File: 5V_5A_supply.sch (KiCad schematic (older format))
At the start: 14 parts, among them U2 TPS54561

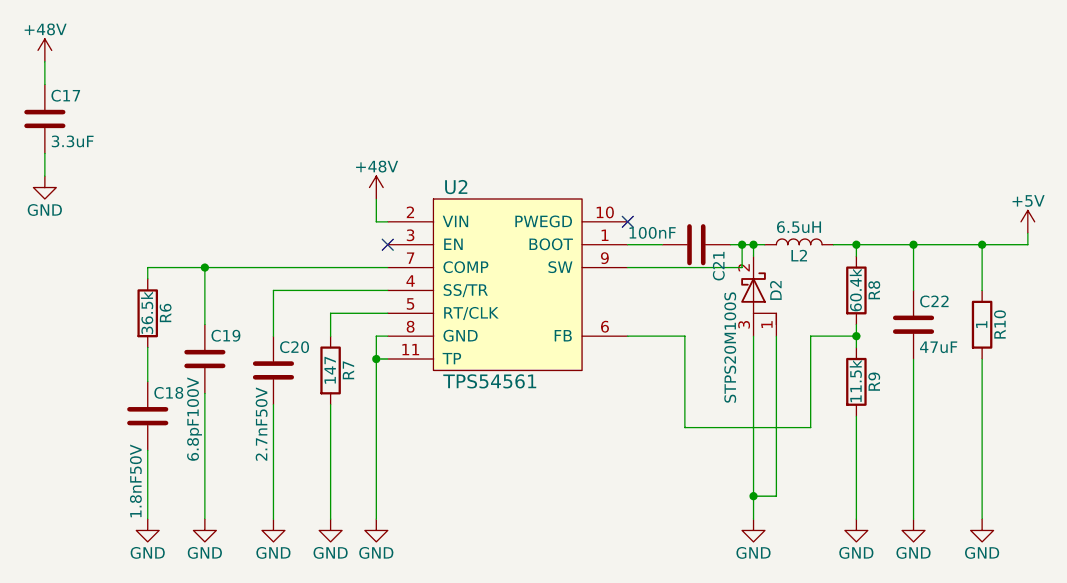
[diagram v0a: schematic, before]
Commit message: add MPN and change footprints
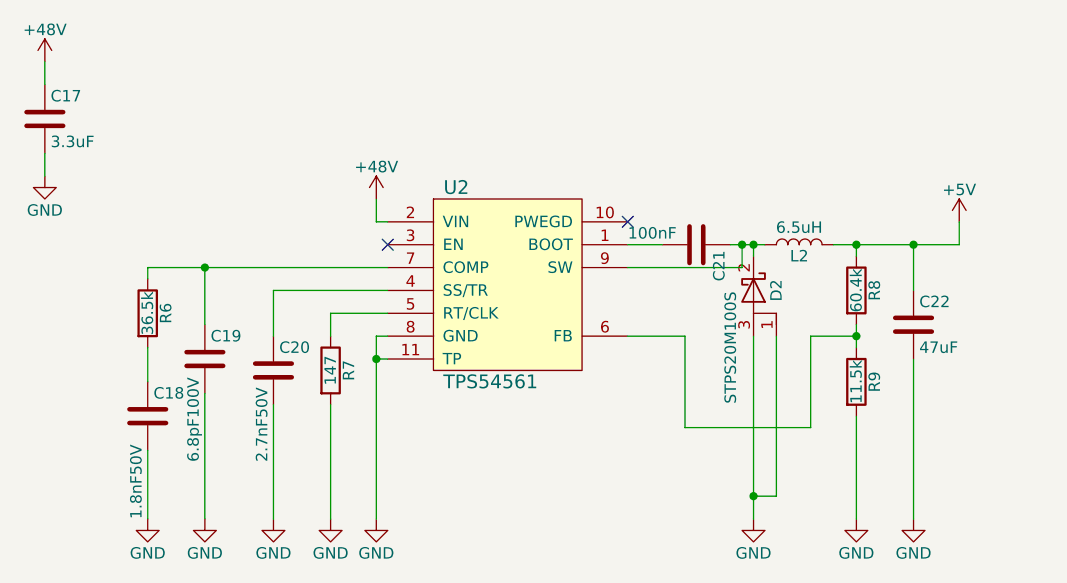
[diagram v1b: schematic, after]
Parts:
- removed R10: 1, Resistors_SMD:R_0402, symbol R
- C17: footprint Capacitors_SMD:C_1206 -> Capacitors_SMD:C_1210; MPN (none) -> 2211157
- C18: MPN (none) -> 2678141
- C19: footprint Capacitors_SMD:C_0402 -> Capacitors_SMD:C_0603; MPN (none) -> 1865503
- C20: footprint Capacitors_SMD:C_0805 -> Capacitors_SMD:C_0603; MPN (none) -> 2680086
- C21: MPN (none) -> 2690952
- C22: footprint Capacitors_SMD:C_1210 -> Capacitors_SMD:C_0603; MPN (none) -> 2346908
- D2: MPN (none) -> 2325907
- L2: MPN (none) -> 2211621
- R6: MPN (none) -> 2072974
- R7: MPN (none) -> 1802949
- R8: MPN (none) -> 1652810
- R9: MPN (none) -> 1803142
- U2: MPN (none) -> TPS54561DPRT
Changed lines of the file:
@@
 LIBS:contrib
 LIBS:valves
+LIBS:MB_DEVICE
 LIBS:power_board-cache
 EELAYER 25 0
@@
 F 2 "MB_LIB:TPS54561" H 5450 3400 60  0001 C CNN
 F 3 "" H 5450 3400 60  0001 C CNN
+F 4 "TPS54561DPRT" H 5450 3400 60  0001 C CNN "MPN"
 	1    5450 3400
 	1    0    0    -1
@@
 Connection ~ 4900 3650
 $Comp
-L GND #PWR036
+L GND #PWR045
 U 1 1 5AA70352
 P 4900 4350
-F 0 "#PWR036" H 4900 4100 50  0001 C CNN
+F 0 "#PWR045" H 4900 4100 50  0001 C CNN
 F 1 "GND" H 4900 4200 50  0000 C CNN
 F 2 "" H 4900 4350 50  0001 C CNN
@@
 F 0 "C17" H 3475 2700 50  0000 L CNN
 F 1 "3.3uF" H 3475 2500 50  0000 L CNN
-F 2 "Capacitors_SMD:C_1206" H 3488 2450 50  0001 C CNN
+F 2 "Capacitors_SMD:C_1210" H 3488 2450 50  0001 C CNN
 F 3 "" H 3450 2600 50  0001 C CNN
+F 4 "2211157" H 3450 2600 60  0001 C CNN "MPN"
 	1    3450 2600
 	1    0    0    -1
@@
 F 2 "Capacitors_SMD:C_0402" H 3938 3750 50  0001 C CNN
 F 3 "" H 3900 3900 50  0001 C CNN
+F 4 "2678141" H 3900 3900 60  0001 C CNN "MPN"
 	1    3900 3900
 	1    0    0    -1
@@
 F 0 "C19" H 4175 3750 50  0000 L CNN
 F 1 "6.8pF100V" V 4100 3200 50  0000 L CNN
-F 2 "Capacitors_SMD:C_0402" H 4188 3500 50  0001 C CNN
+F 2 "Capacitors_SMD:C_0603" H 4188 3500 50  0001 C CNN
 F 3 "" H 4150 3650 50  0001 C CNN
+F 4 "1865503" H 4150 3650 60  0001 C CNN "MPN"
 	1    4150 3650
 	1    0    0    -1
@@
 F 0 "C20" H 4475 3800 50  0000 L CNN
 F 1 "2.7nF50V" V 4400 3300 50  0000 L CNN
-F 2 "Capacitors_SMD:C_0805" H 4488 3550 50  0001 C CNN
+F 2 "Capacitors_SMD:C_0603" H 4488 3550 50  0001 C CNN
 F 3 "" H 4450 3700 50  0001 C CNN
+F 4 "2680086" H 4450 3700 60  0001 C CNN "MPN"
 	1    4450 3700
 	1    0    0    -1
@@
 F 2 "Resistors_SMD:R_0402" V 3830 3450 50  0001 C CNN
 F 3 "" H 3900 3450 50  0001 C CNN
+F 4 "2072974" V 3900 3450 60  0001 C CNN "MPN"
 	1    3900 3450
 	1    0    0    -1
@@
 F 2 "Resistors_SMD:R_0402" V 4630 3700 50  0001 C CNN
 F 3 "" H 4700 3700 50  0001 C CNN
+F 4 "1802949" V 4700 3700 60  0001 C CNN "MPN"
 	1    4700 3700
 	1    0    0    -1
@@
 F 2 "Capacitors_SMD:C_0402" H 6338 3000 50  0001 C CNN
 F 3 "" H 6300 3150 50  0001 C CNN
+F 4 "2690952" H 6300 3150 60  0001 C CNN "MPN"
 	1    6300 3150
 	0    1    1    0
@@
 F 2 "Resistors_SMD:R_0402" V 6930 3350 50  0001 C CNN
 F 3 "" H 7000 3350 50  0001 C CNN
+F 4 "1652810" V 7000 3350 60  0001 C CNN "MPN"
 	1    7000 3350
 	1    0    0    -1
@@
 F 2 "Resistors_SMD:R_0402" V 6930 3750 50  0001 C CNN
 F 3 "" H 7000 3750 50  0001 C CNN
+F 4 "1803142" V 7000 3750 60  0001 C CNN "MPN"
 	1    7000 3750
 	1    0    0    -1
 $EndComp
 $Comp
-L +48V #PWR037
+L +48V #PWR046
 U 1 1 5AA7035C
 P 3450 2350
-F 0 "#PWR037" H 3450 2200 50  0001 C CNN
+F 0 "#PWR046" H 3450 2200 50  0001 C CNN
 F 1 "+48V" H 3450 2490 50  0000 C CNN
 F 2 "" H 3450 2350 50  0001 C CNN
@@
 $EndComp
 $Comp
-L +48V #PWR038
+L +48V #PWR047
 U 1 1 5AA7035D
 P 4900 2950
-F 0 "#PWR038" H 4900 2800 50  0001 C CNN
+F 0 "#PWR047" H 4900 2800 50  0001 C CNN
 F 1 "+48V" H 4900 3090 50  0000 C CNN
 F 2 "" H 4900 2950 50  0001 C CNN
@@
 $EndComp
 $Comp
-L GND #PWR039
+L GND #PWR048
 U 1 1 5AA7035E
 P 3450 2850
-F 0 "#PWR039" H 3450 2600 50  0001 C CNN
+F 0 "#PWR048" H 3450 2600 50  0001 C CNN
 F 1 "GND" H 3450 2700 50  0000 C CNN
 F 2 "" H 3450 2850 50  0001 C CNN
@@
 	4700 3850 4700 4350
 $Comp
-L GND #PWR040
+L GND #PWR049
 U 1 1 5AA7035F
 P 4700 4350
-F 0 "#PWR040" H 4700 4100 50  0001 C CNN
+F 0 "#PWR049" H 4700 4100 50  0001 C CNN
 F 1 "GND" H 4700 4200 50  0000 C CNN
 F 2 "" H 4700 4350 50  0001 C CNN
@@
 $EndComp
 $Comp
-L GND #PWR041
+L GND #PWR050
 U 1 1 5AA70360
 P 4450 4350
-F 0 "#PWR041" H 4450 4100 50  0001 C CNN
+F 0 "#PWR050" H 4450 4100 50  0001 C CNN
 F 1 "GND" H 4450 4200 50  0000 C CNN
 F 2 "" H 4450 4350 50  0001 C CNN
@@
 $EndComp
 $Comp
-L GND #PWR042
+L GND #PWR051
 U 1 1 5AA70361
 P 4150 4350
-F 0 "#PWR042" H 4150 4100 50  0001 C CNN
+F 0 "#PWR051" H 4150 4100 50  0001 C CNN
 F 1 "GND" H 4150 4200 50  0000 C CNN
 F 2 "" H 4150 4350 50  0001 C CNN
@@
 $EndComp
 $Comp
-L GND #PWR043
+L GND #PWR052
 U 1 1 5AA70362
 P 3900 4350
-F 0 "#PWR043" H 3900 4100 50  0001 C CNN
+F 0 "#PWR052" H 3900 4100 50  0001 C CNN
 F 1 "GND" H 3900 4200 50  0000 C CNN
 F 2 "" H 3900 4350 50  0001 C CNN
@@
 F 2 "Inductors_SMD:L_Wuerth_HCI-1050" H 6750 3150 50  0001 C CNN
 F 3 "http://katalog.we-online.de/pbs/datasheet/744325650.pdf" H 6750 3150 50  0001 C CNN
+F 4 "2211621" V 6750 3150 60  0001 C CNN "MPN"
 	1    6750 3150
 	0    -1   -1   0
@@
 Connection ~ 7000 3150
 Wire Wire Line
-	6900 3150 7750 3150
+	6900 3150 7450 3150
 Wire Wire Line
 	7250 3150 7250 3350
 Wire Wire Line
 	7250 3650 7250 4350
-$Comp
-L R R10
-U 1 1 5AA70366
-P 7550 3500
-F 0 "R10" V 7630 3500 50  0000 C CNN
-F 1 "1" V 7550 3500 50  0000 C CNN
-F 2 "Resistors_SMD:R_0402" V 7480 3500 50  0001 C CNN
-F 3 "" H 7550 3500 50  0001 C CNN
-	1    7550 3500
-	1    0    0    -1
-$EndComp
-Wire Wire Line
-	7550 3150 7550 3350
 Connection ~ 7250 3150
-Wire Wire Line
-	7550 3650 7550 4350
 Wire Wire Line
 	6000 3250 6500 3250
@@
 Connection ~ 6550 3150
 $Comp
-L GND #PWR044
+L GND #PWR053
 U 1 1 5AA70368
 P 6550 4350
-F 0 "#PWR044" H 6550 4100 50  0001 C CNN
+F 0 "#PWR053" H 6550 4100 50  0001 C CNN
 F 1 "GND" H 6550 4200 50  0000 C CNN
 F 2 "" H 6550 4350 50  0001 C CNN
@@
 	7000 3900 7000 4350
 $Comp
-L GND #PWR045
+L GND #PWR054
 U 1 1 5AA70369
 P 7000 4350
-F 0 "#PWR045" H 7000 4100 50  0001 C CNN
+F 0 "#PWR054" H 7000 4100 50  0001 C CNN
 F 1 "GND" H 7000 4200 50  0000 C CNN
 F 2 "" H 7000 4350 50  0001 C CNN
@@
 $EndComp
 $Comp
-L GND #PWR046
+L GND #PWR055
 U 1 1 5AA7036A
 P 7250 4350
-F 0 "#PWR046" H 7250 4100 50  0001 C CNN
+F 0 "#PWR055" H 7250 4100 50  0001 C CNN
 F 1 "GND" H 7250 4200 50  0000 C CNN
 F 2 "" H 7250 4350 50  0001 C CNN
@@
 	1    0    0    -1
 $EndComp
-$Comp
-L GND #PWR047
-U 1 1 5AA7036B
-P 7550 4350
-F 0 "#PWR047" H 7550 4100 50  0001 C CNN
-F 1 "GND" H 7550 4200 50  0000 C CNN
-F 2 "" H 7550 4350 50  0001 C CNN
-F 3 "" H 7550 4350 50  0001 C CNN
-	1    7550 4350
-	1    0    0    -1
-$EndComp
-Wire Wire Line
-	7750 3150 7750 3100
-Connection ~ 7550 3150
+Wire Wire Line
+	7450 3150 7450 3050
 $Comp
 L C C22
@@
 F 0 "C22" H 7275 3600 50  0000 L CNN
 F 1 "47uF" H 7275 3400 50  0000 L CNN
-F 2 "Capacitors_SMD:C_1210" H 7288 3350 50  0001 C CNN
+F 2 "Capacitors_SMD:C_0603" H 7288 3350 50  0001 C CNN
 F 3 "" H 7250 3500 50  0001 C CNN
+F 4 "2346908" H 7250 3500 60  0001 C CNN "MPN"
 	1    7250 3500
 	1    0    0    -1
 $EndComp
 $Comp
-L +5V #PWR048
+L +5V #PWR056
 U 1 1 5AA707C6
-P 7750 3100
-F 0 "#PWR048" H 7750 2950 50  0001 C CNN
-F 1 "+5V" H 7750 3240 50  0000 C CNN
-F 2 "" H 7750 3100 50  0001 C CNN
-F 3 "" H 7750 3100 50  0001 C CNN
-	1    7750 3100
+P 7450 3050
+F 0 "#PWR056" H 7450 2900 50  0001 C CNN
+F 1 "+5V" H 7450 3190 50  0000 C CNN
+F 2 "" H 7450 3050 50  0001 C CNN
+F 3 "" H 7450 3050 50  0001 C CNN
+	1    7450 3050
 	1    0    0    -1
 $EndComp
@@
 F 2 "TO_SOT_Packages_SMD:TO-263-2" H 6550 3350 50  0001 C CNN
 F 3 "http://www.st.com/content/ccc/resource/technical/document/datasheet/group2/8f/d3/41/ea/82/b2/4b/5a/CD00228904/files/CD00228904.pdf/jcr:content/translations/en.CD00228904.pdf" H 6550 3350 50  0001 C CNN
+F 4 "2325907" H 6550 3350 60  0001 C CNN "MPN"
 	1    6550 3350
 	0    1    1    0

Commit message: mpn was changed
added needed conectors
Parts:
- C17: MPN 2211157 -> CGA6P3X7R1H335K250AB
- C18: MPN 2678141 -> C0402C182J5RACTU
- C19: MPN 1865503 -> C0603C689C1GACTU
- C20: MPN 2680086 -> C0603C272J5RACTU
- C21: MPN 2690952 -> 04025C104KAT2A
- C22: MPN 2346908 -> C1608X7R1H474K080AC
- D2: MPN 2325907 -> STPS20M100SG-TR
- L2: MPN 2211621 -> 744325650
- R6: MPN 2072974 -> MCMR04X3652FTL
- R7: MPN 1802949 -> MC00625W04021147R
- R8: MPN 1652810 -> CRCW040260K4FKED
- R9: MPN 1803142 -> MC00625W0402111K5
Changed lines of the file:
@@
 F 2 "Capacitors_SMD:C_1210" H 3488 2450 50  0001 C CNN
 F 3 "" H 3450 2600 50  0001 C CNN
-F 4 "2211157" H 3450 2600 60  0001 C CNN "MPN"
+F 4 "CGA6P3X7R1H335K250AB" H 3450 2600 60  0001 C CNN "MPN"
 	1    3450 2600
 	1    0    0    -1
@@
 F 2 "Capacitors_SMD:C_0402" H 3938 3750 50  0001 C CNN
 F 3 "" H 3900 3900 50  0001 C CNN
-F 4 "2678141" H 3900 3900 60  0001 C CNN "MPN"
+F 4 "C0402C182J5RACTU" H 3900 3900 60  0001 C CNN "MPN"
 	1    3900 3900
 	1    0    0    -1
@@
 F 2 "Capacitors_SMD:C_0603" H 4188 3500 50  0001 C CNN
 F 3 "" H 4150 3650 50  0001 C CNN
-F 4 "1865503" H 4150 3650 60  0001 C CNN "MPN"
+F 4 "C0603C689C1GACTU" H 4150 3650 60  0001 C CNN "MPN"
 	1    4150 3650
 	1    0    0    -1
@@
 F 2 "Capacitors_SMD:C_0603" H 4488 3550 50  0001 C CNN
 F 3 "" H 4450 3700 50  0001 C CNN
-F 4 "2680086" H 4450 3700 60  0001 C CNN "MPN"
+F 4 "C0603C272J5RACTU" H 4450 3700 60  0001 C CNN "MPN"
 	1    4450 3700
 	1    0    0    -1
@@
 F 2 "Resistors_SMD:R_0402" V 3830 3450 50  0001 C CNN
 F 3 "" H 3900 3450 50  0001 C CNN
-F 4 "2072974" V 3900 3450 60  0001 C CNN "MPN"
+F 4 "MCMR04X3652FTL" V 3900 3450 60  0001 C CNN "MPN"
 	1    3900 3450
 	1    0    0    -1
@@
 F 2 "Resistors_SMD:R_0402" V 4630 3700 50  0001 C CNN
 F 3 "" H 4700 3700 50  0001 C CNN
-F 4 "1802949" V 4700 3700 60  0001 C CNN "MPN"
+F 4 "MC00625W04021147R" V 4700 3700 60  0001 C CNN "MPN"
 	1    4700 3700
 	1    0    0    -1
@@
 F 2 "Capacitors_SMD:C_0402" H 6338 3000 50  0001 C CNN
 F 3 "" H 6300 3150 50  0001 C CNN
-F 4 "2690952" H 6300 3150 60  0001 C CNN "MPN"
+F 4 "04025C104KAT2A" H 6300 3150 60  0001 C CNN "MPN"
 	1    6300 3150
 	0    1    1    0
@@
 F 2 "Resistors_SMD:R_0402" V 6930 3350 50  0001 C CNN
 F 3 "" H 7000 3350 50  0001 C CNN
-F 4 "1652810" V 7000 3350 60  0001 C CNN "MPN"
+F 4 "CRCW040260K4FKED" V 7000 3350 60  0001 C CNN "MPN"
 	1    7000 3350
 	1    0    0    -1
@@
 F 2 "Resistors_SMD:R_0402" V 6930 3750 50  0001 C CNN
 F 3 "" H 7000 3750 50  0001 C CNN
-F 4 "1803142" V 7000 3750 60  0001 C CNN "MPN"
+F 4 "MC00625W0402111K5" V 7000 3750 60  0001 C CNN "MPN"
 	1    7000 3750
 	1    0    0    -1
@@
 F 2 "Inductors_SMD:L_Wuerth_HCI-1050" H 6750 3150 50  0001 C CNN
 F 3 "http://katalog.we-online.de/pbs/datasheet/744325650.pdf" H 6750 3150 50  0001 C CNN
-F 4 "2211621" V 6750 3150 60  0001 C CNN "MPN"
+F 4 "744325650" V 6750 3150 60  0001 C CNN "MPN"
 	1    6750 3150
 	0    -1   -1   0
@@
 F 2 "Capacitors_SMD:C_0603" H 7288 3350 50  0001 C CNN
 F 3 "" H 7250 3500 50  0001 C CNN
-F 4 "2346908" H 7250 3500 60  0001 C CNN "MPN"
+F 4 "C1608X7R1H474K080AC" H 7250 3500 60  0001 C CNN "MPN"
 	1    7250 3500
 	1    0    0    -1
@@
 F 2 "TO_SOT_Packages_SMD:TO-263-2" H 6550 3350 50  0001 C CNN
 F 3 "http://www.st.com/content/ccc/resource/technical/document/datasheet/group2/8f/d3/41/ea/82/b2/4b/5a/CD00228904/files/CD00228904.pdf/jcr:content/translations/en.CD00228904.pdf" H 6550 3350 50  0001 C CNN
-F 4 "2325907" H 6550 3350 60  0001 C CNN "MPN"
+F 4 "STPS20M100SG-TR" H 6550 3350 60  0001 C CNN "MPN"
 	1    6550 3350
 	0    1    1    0

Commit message: fixed
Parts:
- C22: footprint Capacitors_SMD:C_0603 -> Capacitor_SMD:C_1206_3216Metric_Pad1.24x1.80mm_HandSolder; MPN C1608X7R1H474K080AC -> CL31A476MQHNNNE
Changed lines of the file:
@@
 F 0 "C22" H 7275 3600 50  0000 L CNN
 F 1 "47uF" H 7275 3400 50  0000 L CNN
-F 2 "Capacitors_SMD:C_0603" H 7288 3350 50  0001 C CNN
+F 2 "Capacitor_SMD:C_1206_3216Metric_Pad1.24x1.80mm_HandSolder" H 7288 3350 50  0001 C CNN
 F 3 "" H 7250 3500 50  0001 C CNN
-F 4 "C1608X7R1H474K080AC" H 7250 3500 60  0001 C CNN "MPN"
+F 4 "CL31A476MQHNNNE" H 7250 3500 60  0001 C CNN "MPN"
 	1    7250 3500
 	1    0    0    -1

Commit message: kicost file added
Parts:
- R6: MPN MCMR04X3652FTL -> RC0402FR-0736K5L
- R7: MPN MC00625W04021147R -> ERJ-2RKF1470X
- R9: MPN MC00625W0402111K5 -> RC0402FR-0711K5L
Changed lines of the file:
@@
 LIBS:contrib
 LIBS:valves
-LIBS:MB_DEVICE
 LIBS:power_board-cache
 EELAYER 25 0
@@
 F 2 "Resistors_SMD:R_0402" V 3830 3450 50  0001 C CNN
 F 3 "" H 3900 3450 50  0001 C CNN
-F 4 "MCMR04X3652FTL" V 3900 3450 60  0001 C CNN "MPN"
+F 4 "RC0402FR-0736K5L " V 3900 3450 60  0001 C CNN "MPN"
 	1    3900 3450
 	1    0    0    -1
@@
 F 2 "Resistors_SMD:R_0402" V 4630 3700 50  0001 C CNN
 F 3 "" H 4700 3700 50  0001 C CNN
-F 4 "MC00625W04021147R" V 4700 3700 60  0001 C CNN "MPN"
+F 4 "ERJ-2RKF1470X " V 4700 3700 60  0001 C CNN "MPN"
 	1    4700 3700
 	1    0    0    -1
@@
 F 2 "Resistors_SMD:R_0402" V 6930 3750 50  0001 C CNN
 F 3 "" H 7000 3750 50  0001 C CNN
-F 4 "MC00625W0402111K5" V 7000 3750 60  0001 C CNN "MPN"
+F 4 "RC0402FR-0711K5L" V 7000 3750 60  0001 C CNN "MPN"
 	1    7000 3750
 	1    0    0    -1
